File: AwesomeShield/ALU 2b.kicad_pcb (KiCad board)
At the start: 2 copper layers, 82 parts, among them J1 CONN_01X04, J2 CONN_01X04, J3 CONN_01X03, J4 CONN_01X08, J5 CONN_01X01, J6 CONN_01X04, U1 74LS08, U10 LM741, U2 74LS08, U3 74LS08, U4 74LS83, U5 74LS83, U6 74LS83, U7 74LS244, U8 LM741, U9 LM741

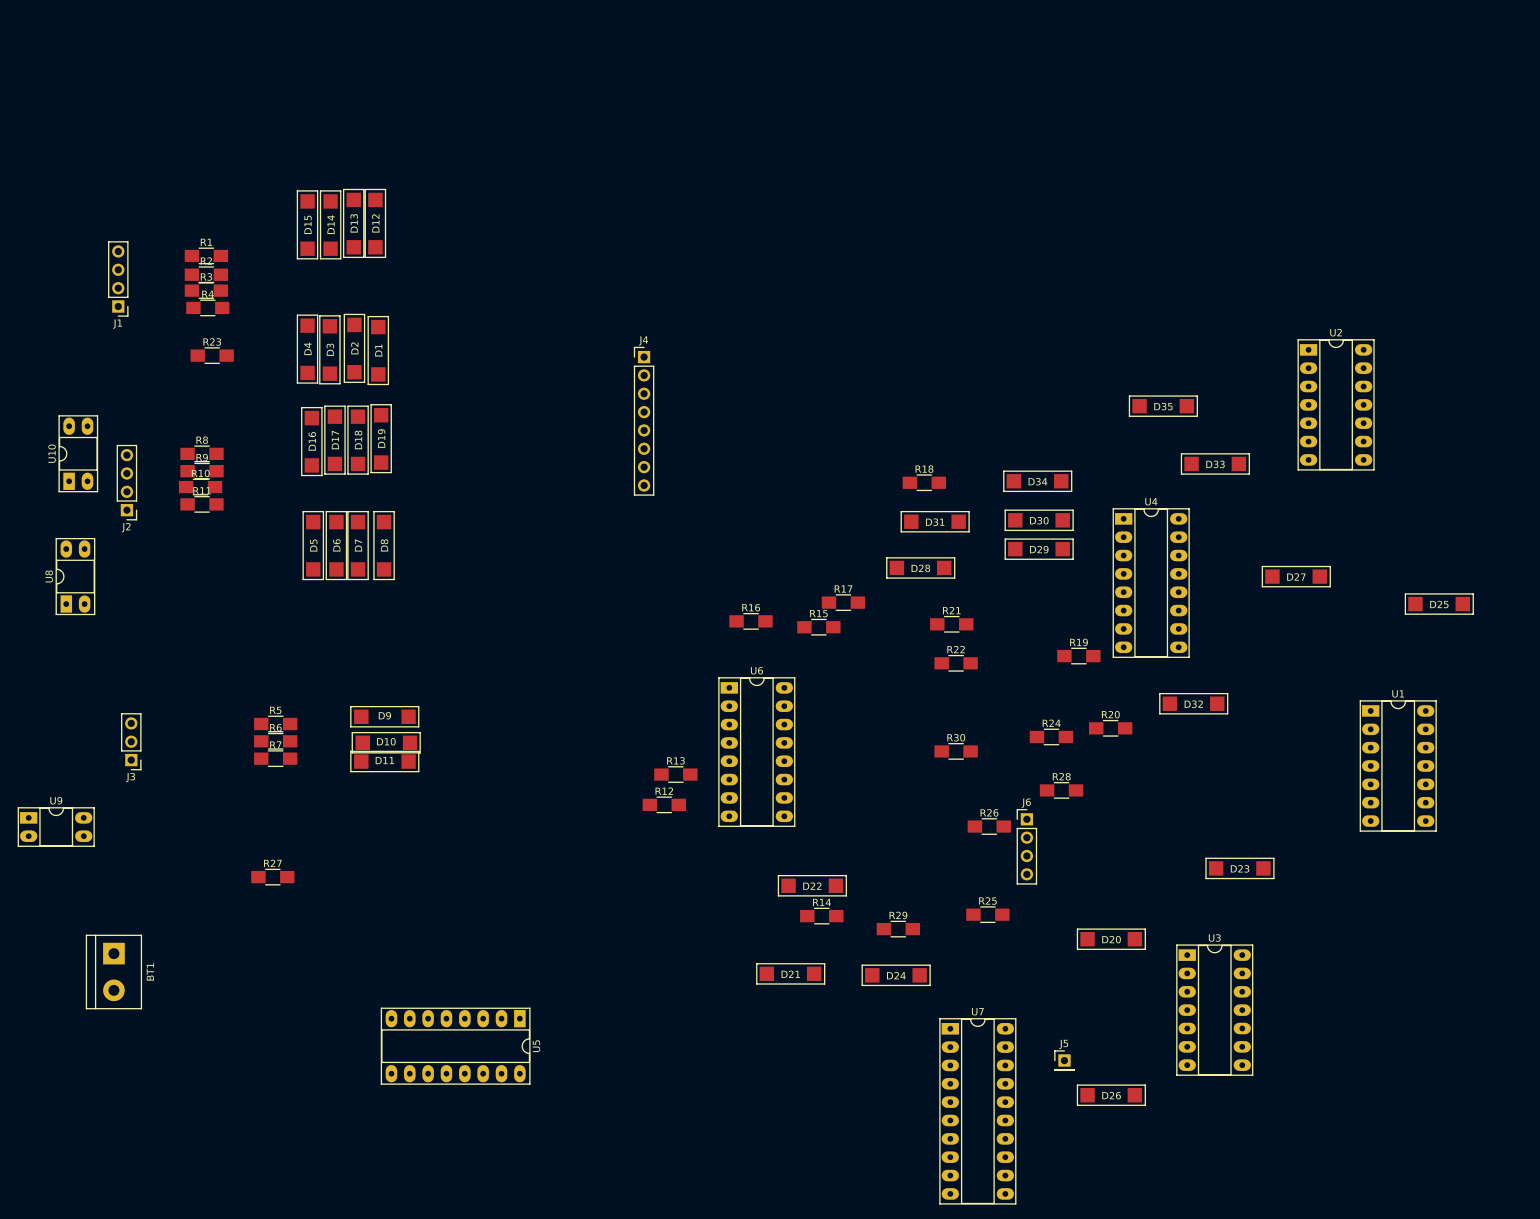
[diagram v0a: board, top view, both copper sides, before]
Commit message: Added pcb file for shield
Assigned remaining footprints and made first layout iteration
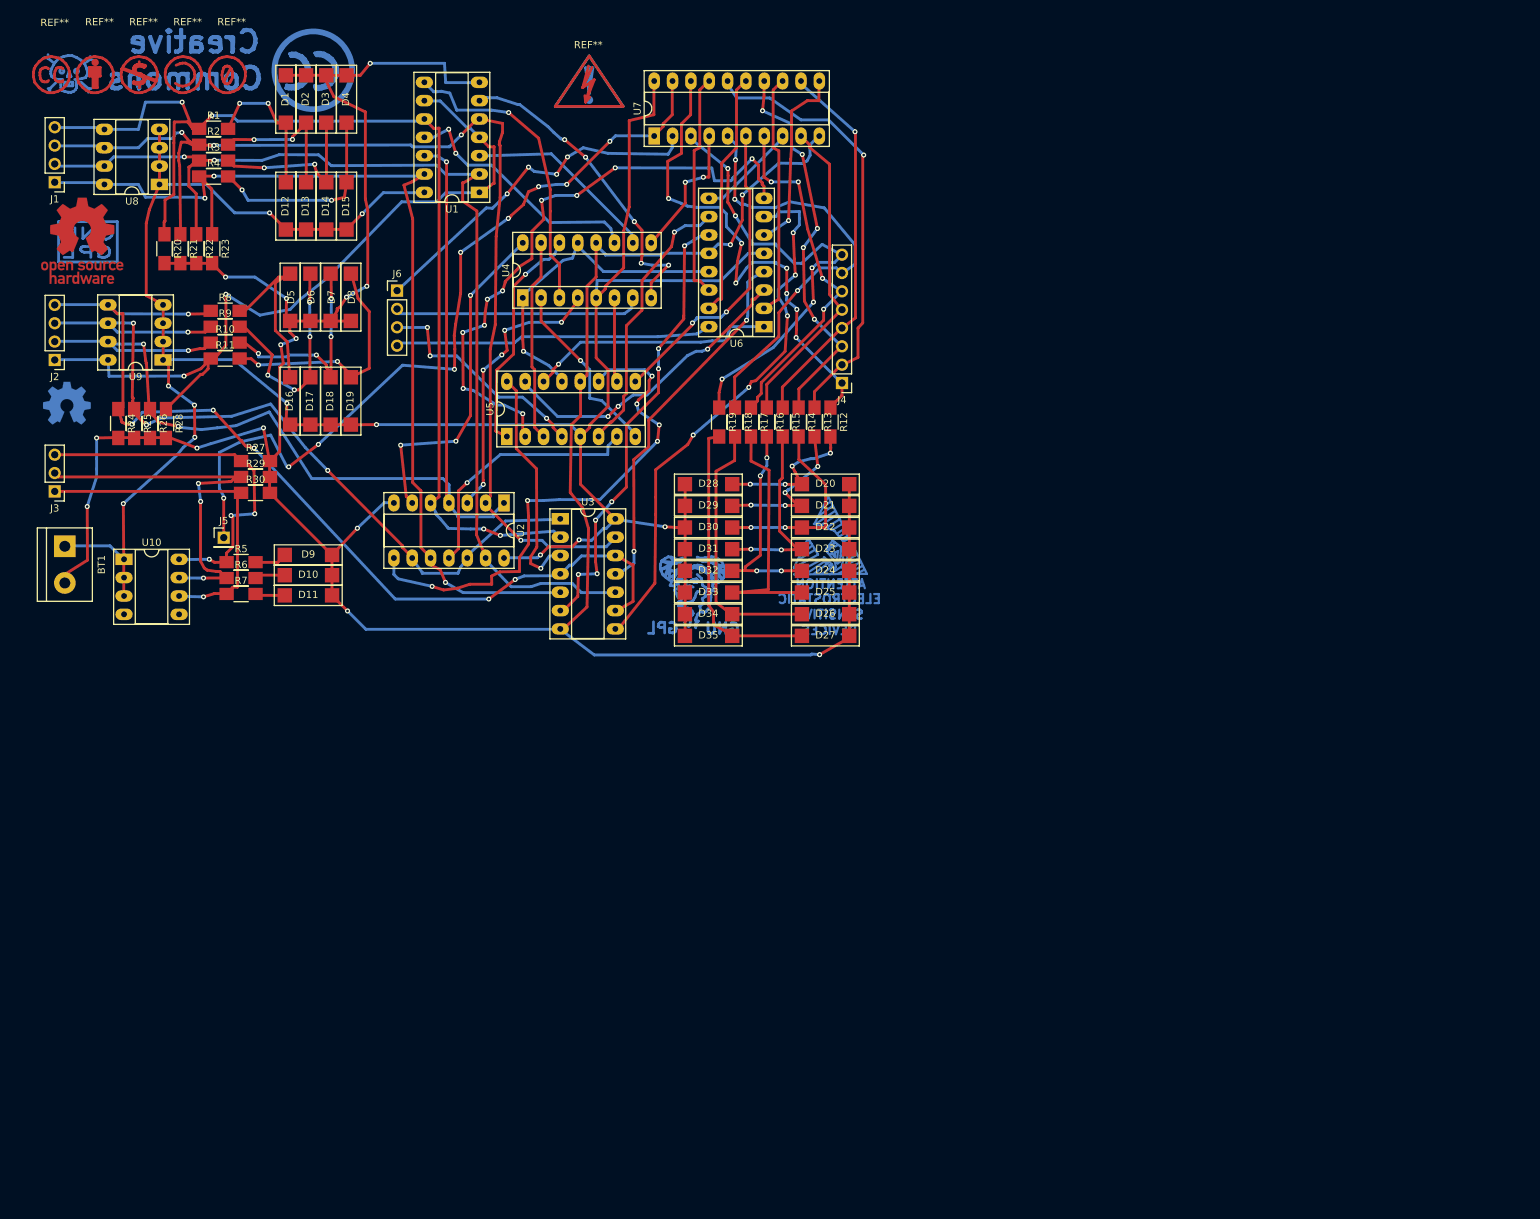
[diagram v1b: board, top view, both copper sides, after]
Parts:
- added REF**: Symbol_CC-Attribution_CopperTop_Small, Symbols:Symbol_CC-Attribution_CopperTop_Small, F.Cu at (25.0, 14.9)
- added REF**: Symbol_CreativeCommons_CopperTop_Type1_Big, Symbols:Symbol_CreativeCommons_CopperTop_Type1_Big, B.Cu at (55.2, 14.3)
- added REF**: Symbol_ESD-Logo-Text_CopperTop, Symbols:Symbol_ESD-Logo-Text_CopperTop, B.Cu at (126.7, 80.7)
- added REF**: Symbol_Danger_CopperTop_Small, Symbols:Symbol_Danger_CopperTop_Small, B.Cu at (21.4, 14.8)
- added REF**: Symbol_CC-Noncommercial_CopperTop_Small, Symbols:Symbol_CC-Noncommercial_CopperTop_Small, F.Cu at (31.1, 14.9)
- added REF**: Symbol_CreativeCommons_CopperTop_Type2_Small, Symbols:Symbol_CreativeCommons_CopperTop_Type2_Small, F.Cu at (18.8, 15.0)
- added REF**: Symbol_HighVoltage_Type2_CopperTop_VerySmall, Symbols:Symbol_HighVoltage_Type2_CopperTop_VerySmall, F.Cu at (93.4, 16.5)
- added REF**: Symbol_Attention_CopperTop_Small, Symbols:Symbol_Attention_CopperTop_Small, B.Cu at (93.4, 16.5)
- added REF**: Symbol_GNU-GPL_CopperTop_Small, Symbols:Symbol_GNU-GPL_CopperTop_Small, B.Cu at (24.0, 38.3)
- added REF**: Symbol_CC-ShareAlike_CopperTop_Small, Symbols:Symbol_CC-ShareAlike_CopperTop_Small, F.Cu at (37.2, 14.9)
- added REF**: Symbol_CC-PublicDomain_CopperTop_Small, Symbols:Symbol_CC-PublicDomain_CopperTop_Small, F.Cu at (43.3, 14.9)
- added REF**: Symbol_GNU-Logo_CopperTop, Symbols:Symbol_GNU-Logo_CopperTop, B.Cu at (107.5, 85.4)
- added REF***: OSHW-Logo_11.4x12mm_Copper, Symbols:OSHW-Logo_11.4x12mm_Copper, F.Cu at (23.2, 37.9)
- added REF***: OSHW-Symbol_6.7x6mm_Copper, Symbols:OSHW-Symbol_6.7x6mm_Copper, B.Cu at (21.1, 60.4)
- U10, U8, U9: footprint Housings_DIP:DIP-4_W7.62mm_Socket_LongPads -> Housings_DIP:DIP-8_W7.62mm_Socket_LongPads
- moved R20 146.9 mm to (34.6, 39.0), turned to 270 degrees
- moved U1 142.8 mm to (78.2, 31.2), turned to 180 degrees
- moved J5 137.1 mm to (42.8, 79.0)
- moved R25 136.4 mm to (30.4, 63.2), turned to 270 degrees
- moved R24 136.3 mm to (28.2, 63.2), turned to 270 degrees
- moved R28 134.0 mm to (34.8, 63.2), turned to 270 degrees
- moved U7 130.2 mm to (102.4, 23.4), turned to 90 degrees
- moved R26 128.9 mm to (32.6, 63.2), turned to 270 degrees
- moved R22 119.8 mm to (39.0, 39.0), turned to 270 degrees
- moved R21 118.8 mm to (36.8, 39.0), turned to 270 degrees
- moved J6 113.9 mm to (66.8, 44.8)
- moved U2 113.4 mm to (81.6, 74.2), turned to 270 degrees
- moved R29 108.8 mm to (47.2, 70.6)
- moved U3 105.7 mm to (89.4, 76.4)
- moved R30 103.4 mm to (47.2, 72.8)
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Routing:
- net /Data_A: track 0.00 -> 405.8 mm, vias 0 -> 16
- net Net-(BT1-Pad1): track 0.00 -> 334.7 mm, vias 0 -> 11
- net Net-(J1-Pad3): track 0.00 -> 155.6 mm, vias 0 -> 4
- net Net-(J1-Pad4): track 0.00 -> 154.0 mm, vias 0 -> 4
- net Net-(J1-Pad2): track 0.00 -> 149.1 mm, vias 0 -> 2
- net Net-(J2-Pad2): track 0.00 -> 149.0 mm, vias 0 -> 4
- net Net-(J1-Pad1): track 0.00 -> 142.4 mm, vias 0 -> 3
- net Net-(J2-Pad4): track 0.00 -> 134.2 mm, vias 0 -> 6
- net Net-(J2-Pad3): track 0.00 -> 113.4 mm, vias 0 -> 4
- net Net-(J5-Pad1): track 0.00 -> 111.4 mm, vias 0 -> 9
- net Net-(J2-Pad1): track 0.00 -> 107.2 mm, vias 0 -> 2
- net Net-(U5-Pad2): track 0.00 -> 83.9 mm, vias 0 -> 10
- net Net-(U3-Pad8): track 0.00 -> 75.4 mm, vias 0 -> 5
- net Net-(U2-Pad8): track 0.00 -> 73.3 mm, vias 0 -> 6
- net Net-(J4-Pad1): track 0.00 -> 69.4 mm, vias 0 -> 7
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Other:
- net class Default: trace_width 0.25 -> 0.4; via_dia 0.6 -> 0.7

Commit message: Moved the via under the ICs
Vias under the IC were causing short as discovered upon fabrication of the board.
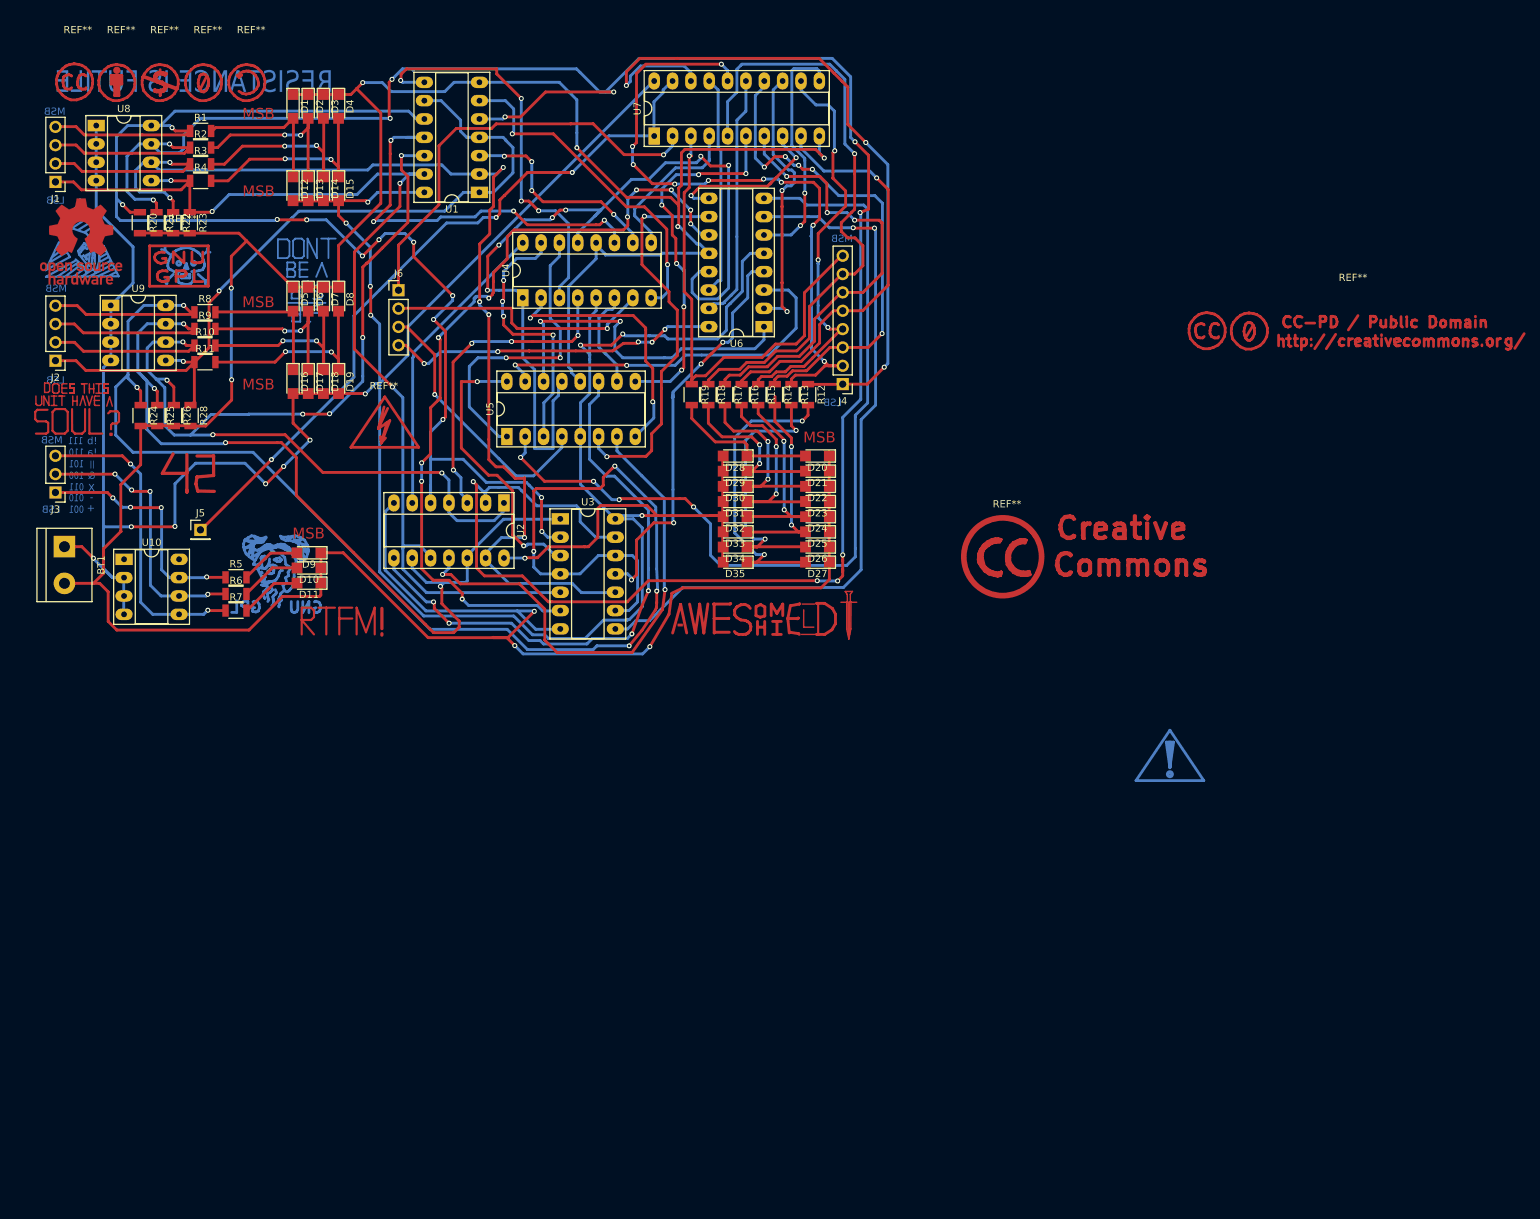
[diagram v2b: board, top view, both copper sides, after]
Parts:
- removed R27, R29, R30: R, Resistors_SMD:R_1206_HandSoldering
- removed the REF** at (126.7, 80.7)
- removed the REF*** at (21.1, 60.4)
- added REF**: Symbol_ESD-Logo_CopperTop, Symbols:Symbol_ESD-Logo_CopperTop, B.Cu at (23.1, 39.5)
- added REF**: Symbol_CreativeCommonsPublicDomain_CopperTop_Small, Symbols:Symbol_CreativeCommonsPublicDomain_CopperTop_Small, F.Cu at (198.6, 50.3)
- D1, D10, D11, D12, D13, D14, D15, D16, D17, D18, D19, D2, D20, D21, D22, D23, D24, D25, D26, D27, D28, D29, D3, D30, D31, D32, D33, D34, D35, D4, D5, D6, D7, D8, D9: footprint LED_5630 footprint:LED_5630 -> LEDs:LED_1206
- R1, R10, R11, R12, R13, R14, R15, R16, R17, R18, R19, R2, R20, R21, R22, R23, R24, R25, R26, R28, R3, R4, R5, R6, R7, R8, R9: footprint Resistors_SMD:R_1206_HandSoldering -> Resistors_SMD:R_1206
- REF** (x2): moved to F.Cu
- moved REF** 123.2 mm to (173.8, 109.8)
- moved REF** 116.8 mm to (150.7, 81.7), turned to 0 degrees
- moved REF** 57.8 mm to (49.8, 82.5)
- moved REF** 55.0 mm to (65.1, 63.7)
- moved REF** 31.1 mm to (37.6, 41.4)
- moved REF** 13.0 mm to (36.6, 41.6), turned to 0 degrees
- moved U8 12.0 mm to (25.1, 21.9), turned to 0 degrees
- moved D27 11.1 mm to (125.0, 82.4)
- moved U9 10.5 mm to (27.1, 46.9), turned to 0 degrees
- moved D26 10.3 mm to (125.0, 80.3)
- moved D35 10.2 mm to (113.6, 82.4)
- moved D25 9.48 mm to (125.0, 78.2)
- moved D34 9.31 mm to (113.6, 80.3)
- moved REF** 8.87 mm to (46.0, 16.0)
- moved D24 8.70 mm to (125.0, 76.1)
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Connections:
- R12 pad 2: Net-(D20-Pad2) -> Net-(D27-Pad2)
- R13 pad 2: Net-(D21-Pad2) -> Net-(D26-Pad2)
- R14 pad 2: Net-(D22-Pad2) -> Net-(D25-Pad2)
- R15 pad 2: Net-(D23-Pad2) -> Net-(D24-Pad2)
- R16 pad 2: Net-(D24-Pad2) -> Net-(D23-Pad2)
- R17 pad 2: Net-(D25-Pad2) -> Net-(D22-Pad2)
- R18 pad 2: Net-(D26-Pad2) -> Net-(D21-Pad2)
- R19 pad 2: Net-(D27-Pad2) -> Net-(D20-Pad2)
- R5 pad 1: Net-(J3-Pad3) -> Net-(J3-Pad1)
- R7 pad 1: Net-(J3-Pad1) -> Net-(J3-Pad3)
- U10 pad 1: Net-(BT1-Pad1) -> Net-(U10-Pad1)
- U10 pad 4: Net-(U10-Pad4) -> Net-(BT1-Pad1)
- U10 pad 5: Net-(U10-Pad5) -> Net-(J3-Pad3)
- U10 pad 6: Net-(J3-Pad1) -> Net-(J3-Pad2)
- U10 pad 7: Net-(J3-Pad2) -> Net-(J3-Pad1)
- U10 pad 8: Net-(J3-Pad3) -> Net-(U10-Pad8)
- U8 pad 5: Net-(J1-Pad4) -> Net-(J1-Pad1)
- U8 pad 6: Net-(J1-Pad3) -> Net-(J1-Pad2)
- U8 pad 7: Net-(J1-Pad2) -> Net-(J1-Pad3)
- U8 pad 8: Net-(J1-Pad1) -> Net-(J1-Pad4)
- U9 pad 5: Net-(J2-Pad4) -> Net-(J2-Pad1)
- U9 pad 6: Net-(J2-Pad3) -> Net-(J2-Pad2)
- U9 pad 7: Net-(J2-Pad2) -> Net-(J2-Pad3)
- U9 pad 8: Net-(J2-Pad1) -> Net-(J2-Pad4)
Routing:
- net (no net): track 0.00 -> 365.4 mm
- net Net-(J1-Pad3): track 155.6 -> 341.8 mm, vias 4 -> 12
- net Net-(BT1-Pad1): track 334.7 -> 465.9 mm, vias 11 -> 15
- net Net-(J2-Pad4): track 134.2 -> 215.7 mm
- net Net-(U4-Pad1): track 46.0 -> 119.3 mm, vias 1 -> 6
- net /Data_A: track 405.8 -> 467.8 mm, vias 16 -> 9
- net Net-(U3-Pad6): track 63.0 -> 111.7 mm, vias 7 -> 10
- net Net-(J1-Pad4): track 154.0 -> 200.7 mm, vias 4 -> 12
- net Net-(U5-Pad2): track 83.9 -> 122.8 mm, vias 10 -> 4
- net Net-(U2-Pad11): track 35.4 -> 70.0 mm, vias 1 -> 2
- net Net-(J2-Pad3): track 113.4 -> 146.5 mm
- net Net-(J4-Pad2): track 61.8 -> 93.2 mm, vias 1 -> 9
- net Net-(J4-Pad1): track 69.4 -> 100.0 mm, vias 7 -> 3
- net Net-(U3-Pad8): track 75.4 -> 101.6 mm, vias 5 -> 2
- net Net-(J4-Pad7): track 61.7 -> 86.7 mm, vias 3 -> 1
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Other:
- net class Default: trace_width 0.4 -> 0.25
- board text added: "!a"
- board text added: "!b"
- board text added: "&"
- board text added: "+"
- board text added: "-"
- board text added: "001"
- board text added: "010"
- board text added: "011"
- board text added: "100"
- board text added: "101"
- board text added: "110"
- board text added: "111"
- board text added: "LSB"
- board text added: "MSB"
- board text added: "RESISTANCE IS FUTILE"
- board text added: "X"
- board text added: "||"

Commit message: Final Design
Final design of both base and shield board which is ready to roll.
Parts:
- removed the REF** at (150.7, 81.7)
- removed the REF** at (198.6, 50.3)
- added REF**: Pin_Header_Straight_1x02_Pitch2.54mm, Pin_Headers:Pin_Header_Straight_1x02_Pitch2.54mm, F.Cu at (16.9, 81.5)
- added REF**: Symbol_CreativeCommons_CopperTop_Type2_Big, Symbols:Symbol_CreativeCommons_CopperTop_Type2_Big, B.Cu at (58.0, 69.0)
- BT1: footprint Connectors:bornier2 -> Pin_Headers:Pin_Header_Straight_1x02_Pitch2.54mm
- moved REF** 63.9 mm to (112.8, 90.9)
- moved REF** 2.90 mm to (49.2, 79.7)
- moved BT1 1.26 mm to (20.6, 81.5), turned to 0 degrees
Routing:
- net (no net): track 365.4 -> 370.9 mm
- net /Data_A: track 467.8 -> 473.0 mm
- net Net-(J2-Pad1): track 110.6 -> 114.5 mm, vias 2 -> 1
- net Net-(BT1-Pad1): track 465.9 -> 463.6 mm
- net Net-(U2-Pad11): track 70.0 -> 70.6 mm
- net Net-(U2-Pad8): track 80.1 -> 80.7 mm
- net Net-(J2-Pad2): track 168.0 -> 168.5 mm
